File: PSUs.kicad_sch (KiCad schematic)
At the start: 33 parts, among them J19 Barrel_Jack, J20 AMP171826-4, Q1 DMP3013SFV-7, U16 AP64501SP-13

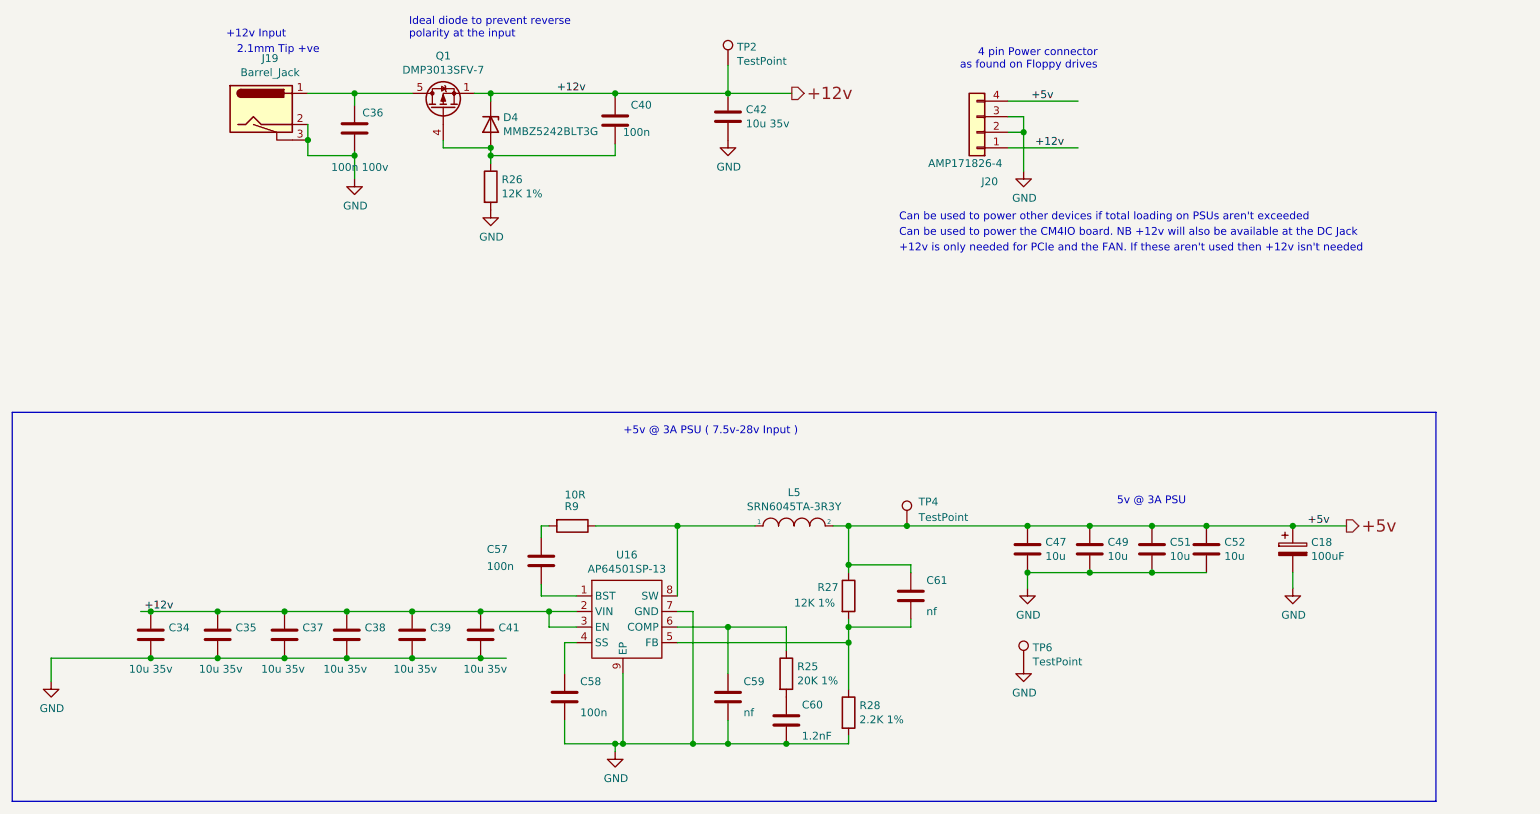
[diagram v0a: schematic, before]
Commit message: Removing unneeded items
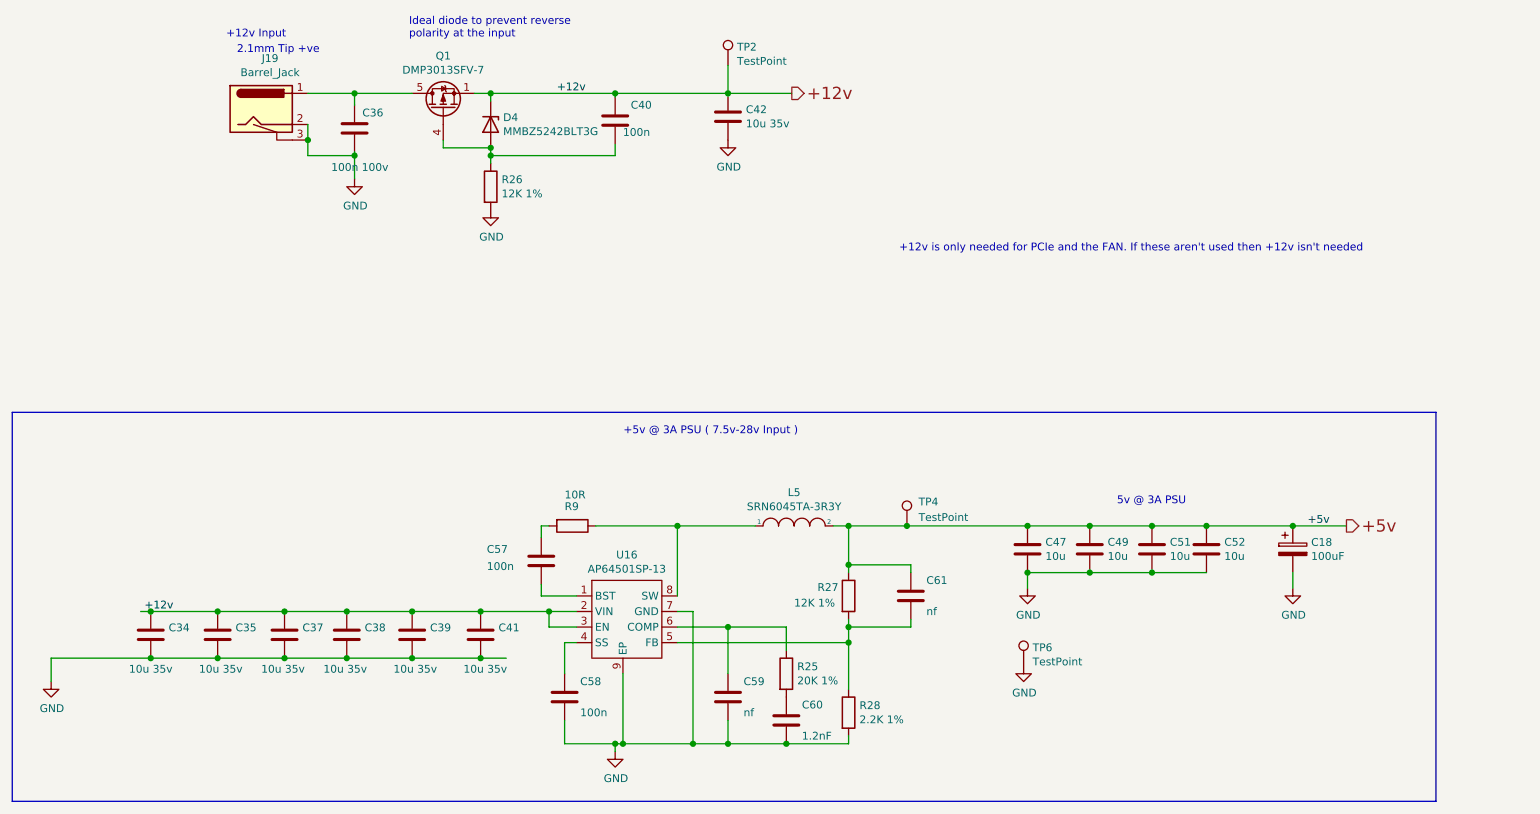
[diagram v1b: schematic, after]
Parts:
- removed J20: AMP171826-4, 171826-4:TE_171826-4, symbol Connector_Generic:Conn_01x04
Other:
- note removed: "4 pin Power connector as found on Floppy drives"
- note removed: "Can be used to power other devices if total loading on PSUs aren't exceeded"
- note removed: "Can be used to power the CM4IO board. NB +12v will also be available at the DC Jack"
